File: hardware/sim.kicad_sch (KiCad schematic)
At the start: 11 parts, among them J12 PRPC006SAAN-RC, J13 SIM8070-6-0-11-00-A

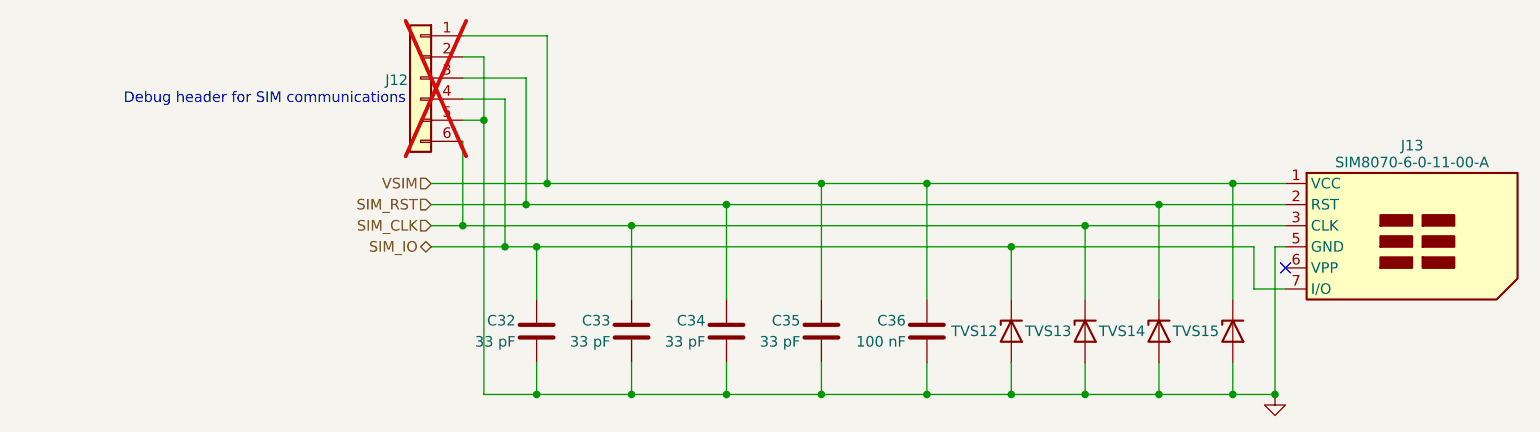
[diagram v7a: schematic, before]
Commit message: HW: Update components, change footprints to handsolder versions, finish power
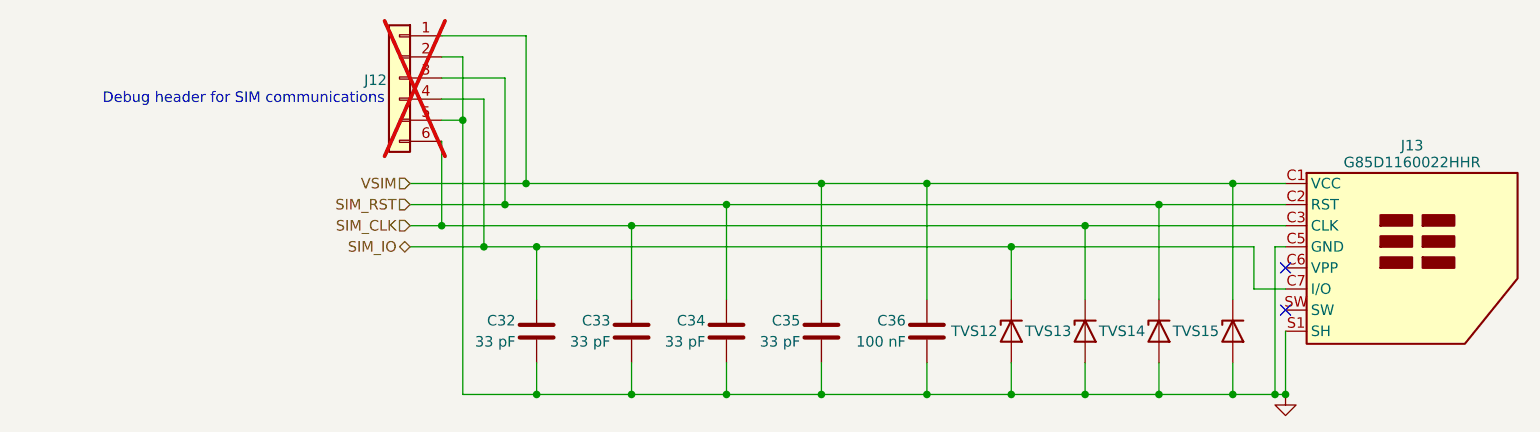
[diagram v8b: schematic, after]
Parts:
- J13: value SIM8070-6-0-11-00-A -> G85D1160022HHR; footprint SIM8070-6-0-11-00-A:SIM8070-6-0-11-00-A -> G85D1160022HHR:AMPHENOL_G85D1160022HHR; Digi-Key Part Number 2073-SIM8070-6-0-11-00-ACT-ND -> 664-G85D1160022HHRCT-ND; Manufacturer GCT -> Amphenol ICC (Commercial Products); Manufacturer Part Number SIM8070-6-0-11-00-A -> G85D1160022HHR
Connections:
- net GND: now also J13.C5 (GND), J13.S1 (SH), J13.S2 (SH), J13.S3 (SH); no longer J13.5 (GND)
- net SIM_CLK: now also J13.C3 (CLK); no longer J13.3 (CLK)
- net SIM_IO: now also J13.C7 (I/O); no longer J13.7 (I/O)
- net SIM_RST: now also J13.C2 (RST); no longer J13.2 (RST)
- net VSIM: now also J13.C1 (VCC); no longer J13.1 (VCC)
- no-connect marks 1 -> 2
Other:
- moved on the sheet: J12
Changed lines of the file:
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@@
 	)
 	(junction
-		(at 92.71 111.76)
+		(at 90.17 111.76)
+		(diameter 0)
+		(color 0 0 0 0)
+	)
+	(junction
+		(at 95.25 121.92)
 		(diameter 0)
 		(color 0 0 0 0)
@@
 	)
 	(junction
-		(at 97.79 121.92)
+		(at 92.71 127)
 		(diameter 0)
 		(color 0 0 0 0)
 	)
 	(junction
-		(at 100.33 119.38)
+		(at 97.79 119.38)
 		(diameter 0)
 		(color 0 0 0 0)
 	)
 	(junction
-		(at 95.25 127)
+		(at 133.35 144.78)
 		(diameter 0)
 		(color 0 0 0 0)
 	)
 	(junction
-		(at 133.35 144.78)
+		(at 182.88 119.38)
 		(diameter 0)
 		(color 0 0 0 0)
 	)
 	(junction
-		(at 182.88 119.38)
+		(at 87.63 124.46)
 		(diameter 0)
 		(color 0 0 0 0)
 	)
 	(junction
-		(at 90.17 124.46)
+		(at 189.23 144.78)
 		(diameter 0)
 		(color 0 0 0 0)
@@
 		(at 189.23 129.54)
 	)
+	(no_connect
+		(at 189.23 134.62)
+	)
 	(wire
 		(pts
-			(xy 97.79 106.68) (xy 97.79 121.92)
+			(xy 95.25 106.68) (xy 95.25 121.92)
 		)
 		(stroke
@@
 	(wire
 		(pts
-			(xy 92.71 144.78) (xy 99.06 144.78)
+			(xy 97.79 119.38) (xy 133.35 119.38)
+		)
+		(stroke
+			(width 0)
+			(type default)
+		)
+	)
+	(wire
+		(pts
+			(xy 90.17 144.78) (xy 99.06 144.78)
 		)
 		(stroke
@@
 	(wire
 		(pts
-			(xy 90.17 106.68) (xy 97.79 106.68)
+			(xy 87.63 106.68) (xy 95.25 106.68)
 		)
 		(stroke
@@
 	(wire
 		(pts
-			(xy 86.36 127) (xy 95.25 127)
+			(xy 83.82 127) (xy 92.71 127)
 		)
 		(stroke
@@
 	(wire
 		(pts
-			(xy 90.17 114.3) (xy 90.17 124.46)
+			(xy 87.63 114.3) (xy 87.63 124.46)
 		)
 		(stroke
@@
 	(wire
 		(pts
-			(xy 86.36 119.38) (xy 100.33 119.38)
+			(xy 83.82 119.38) (xy 97.79 119.38)
 		)
 		(stroke
@@
 	(wire
 		(pts
-			(xy 100.33 101.6) (xy 100.33 119.38)
+			(xy 97.79 101.6) (xy 97.79 119.38)
 		)
 		(stroke
@@
 	(wire
 		(pts
-			(xy 100.33 119.38) (xy 133.35 119.38)
-		)
-		(stroke
-			(width 0)
-			(type default)
-		)
-	)
-	(wire
-		(pts
-			(xy 86.36 124.46) (xy 90.17 124.46)
+			(xy 83.82 124.46) (xy 87.63 124.46)
 		)
 		(stroke
@@
 	(wire
 		(pts
-			(xy 95.25 109.22) (xy 95.25 127)
+			(xy 92.71 109.22) (xy 92.71 127)
 		)
 		(stroke
@@
 	(wire
 		(pts
-			(xy 92.71 111.76) (xy 92.71 144.78)
+			(xy 90.17 111.76) (xy 90.17 144.78)
 		)
 		(stroke
@@
 	(wire
 		(pts
-			(xy 90.17 111.76) (xy 92.71 111.76)
+			(xy 87.63 111.76) (xy 90.17 111.76)
 		)
 		(stroke
@@
 	(wire
 		(pts
-			(xy 90.17 104.14) (xy 92.71 104.14)
+			(xy 87.63 104.14) (xy 90.17 104.14)
 		)
 		(stroke
@@
 	(wire
 		(pts
-			(xy 90.17 109.22) (xy 95.25 109.22)
+			(xy 87.63 109.22) (xy 92.71 109.22)
 		)
 		(stroke
@@
 	(wire
 		(pts
-			(xy 92.71 104.14) (xy 92.71 111.76)
+			(xy 90.17 104.14) (xy 90.17 111.76)
 		)
 		(stroke
@@
 	(wire
 		(pts
-			(xy 97.79 121.92) (xy 121.92 121.92)
+			(xy 165.1 144.78) (xy 173.99 144.78)
 		)
 		(stroke
@@
 	(wire
 		(pts
-			(xy 165.1 144.78) (xy 173.99 144.78)
+			(xy 87.63 101.6) (xy 97.79 101.6)
 		)
 		(stroke
@@
 	(wire
 		(pts
-			(xy 90.17 101.6) (xy 100.33 101.6)
+			(xy 189.23 144.78) (xy 187.96 144.78)
 		)
 		(stroke
@@
 	(wire
 		(pts
+			(xy 95.25 121.92) (xy 121.92 121.92)
+		)
+		(stroke
+			(width 0)
+			(type default)
+		)
+	)
+	(wire
+		(pts
 			(xy 173.99 140.97) (xy 173.99 144.78)
 		)
@@
 	(wire
 		(pts
+			(xy 189.23 137.16) (xy 189.23 144.78)
+		)
+		(stroke
+			(width 0)
+			(type default)
+		)
+	)
+	(wire
+		(pts
 			(xy 156.21 144.78) (xy 165.1 144.78)
 		)
@@
 	(wire
 		(pts
-			(xy 95.25 127) (xy 99.06 127)
+			(xy 92.71 127) (xy 99.06 127)
 		)
 		(stroke
@@
 	(wire
 		(pts
-			(xy 90.17 124.46) (xy 110.49 124.46)
+			(xy 87.63 124.46) (xy 110.49 124.46)
 		)
 		(stroke
@@
 	(wire
 		(pts
-			(xy 86.36 121.92) (xy 97.79 121.92)
+			(xy 83.82 121.92) (xy 95.25 121.92)
 		)
 		(stroke
@@
 	(text "Debug header for SIM communications"
 		(exclude_from_sim no)
-		(at 83.312 109.22 0)
+		(at 80.772 109.22 0)
 		(effects
 			(font
@@
 	(hierarchical_label "VSIM"
 		(shape input)
-		(at 86.36 119.38 180)
+		(at 83.82 119.38 180)
 		(fields_autoplaced yes)
 		(effects
@@
 	(hierarchical_label "SIM_RST"
 		(shape input)
-		(at 86.36 121.92 180)
+		(at 83.82 121.92 180)
 		(fields_autoplaced yes)
 		(effects
@@
 	(hierarchical_label "SIM_CLK"
 		(shape input)
-		(at 86.36 124.46 180)
+		(at 83.82 124.46 180)
 		(fields_autoplaced yes)
 		(effects
@@
 	(hierarchical_label "SIM_IO"
 		(shape bidirectional)
-		(at 86.36 127 180)
+		(at 83.82 127 180)
 		(fields_autoplaced yes)
 		(effects
@@
 	(symbol
 		(lib_id "Connector_Generic:Conn_01x06")
-		(at 85.09 106.68 0)
+		(at 82.55 106.68 0)
 		(mirror y)
 		(unit 1)
@@
 		(dnp yes)
 		(property "Reference" "J12"
-			(at 83.566 106.934 0)
+			(at 81.026 106.934 0)
 			(effects
 				(font
@@
 		)
 		(property "Value" "PRPC006SAAN-RC"
-			(at 83.566 108.712 0)
+			(at 81.026 108.712 0)
 			(effects
 				(font
@@
 		)
 		(property "Footprint" "Connector_PinHeader_2.54mm:PinHeader_1x06_P2.54mm_Vertical"
-			(at 85.09 106.68 0)
+			(at 82.55 106.68 0)
 			(effects
 				(font
@@
 		)
 		(property "Datasheet" "~"
-			(at 85.09 106.68 0)
+			(at 82.55 106.68 0)
 			(effects
 				(font
@@
 		)
 		(property "Description" "Generic connector, single row, 01x06, script generated (kicad-library-utils/schlib/autogen/connector/)"
-			(at 85.09 106.68 0)
+			(at 82.55 106.68 0)
 			(effects
 				(font
@@
 		)
 		(property "Digi-Key Part Number" "S1011EC-06-ND"
-			(at 85.09 106.68 0)
+			(at 82.55 106.68 0)
 			(effects
 				(font
@@
 		)
 		(property "Manufacturer" "Sullins Connector Solutions"
-			(at 85.09 106.68 0)
+			(at 82.55 106.68 0)
 			(effects
 				(font
@@
 		)
 		(property "Manufacturer Part Number" "PRPC006SAAN-RC"
-			(at 85.09 106.68 0)
+			(at 82.55 106.68 0)
 			(effects
 				(font
@@
 			)
 		)
-		(property "Value" "SIM8070-6-0-11-00-A"
+		(property "Value" "G85D1160022HHR"
 			(at 204.47 116.84 0)
 			(effects
@@
 			)
 		)
-		(property "Footprint" "SIM8070-6-0-11-00-A:SIM8070-6-0-11-00-A"
+		(property "Footprint" "G85D1160022HHR:AMPHENOL_G85D1160022HHR"
 			(at 201.93 118.11 0)
 			(effects
@@
 			)
 		)
-		(property "Digi-Key Part Number" "2073-SIM8070-6-0-11-00-ACT-ND"
+		(property "Digi-Key Part Number" "664-G85D1160022HHRCT-ND"
 			(at 201.93 127 0)
 			(effects
@@
 			)
 		)
-		(property "Manufacturer" "GCT"
+		(property "Manufacturer" "Amphenol ICC (Commercial Products)"
 			(at 201.93 127 0)
 			(effects
@@
 			)
 		)
-		(property "Manufacturer Part Number" "SIM8070-6-0-11-00-A"
+		(property "Manufacturer Part Number" "G85D1160022HHR"
 			(at 201.93 127 0)
 			(effects
@@
 			)
 		)
-		(pin "1"
+		(pin "C1"
 		)
-		(pin "2"
+		(pin "C2"
 		)
-		(pin "7"
+		(pin "C3"
 		)
-		(pin "3"
+		(pin "C7"
 		)
-		(pin "5"
+		(pin "S1"
 		)
-		(pin "6"
+		(pin "C5"
+		)
+		(pin "C6"
+		)
+		(pin "S3"
+		)
+		(pin "SW"
+		)
+		(pin "S2"
 		)
 		(instances
@@
 	(symbol
 		(lib_id "power:GND")
-		(at 187.96 144.78 0)
+		(at 189.23 144.78 0)
 		(unit 1)
 		(exclude_from_sim no)
@@
 		(dnp no)
 		(fields_autoplaced yes)
-		(property "Reference" "#PWR058"
-			(at 187.96 151.13 0)
+		(property "Reference" "#PWR056"
+			(at 189.23 151.13 0)
 			(effects
 				(font
@@
 		)
 		(property "Value" "GND"
-			(at 187.96 149.86 0)
+			(at 189.23 149.86 0)
 			(effects
 				(font
@@
 		)
 		(property "Footprint" ""
-			(at 187.96 144.78 0)
+			(at 189.23 144.78 0)
 			(effects
 				(font
@@
 		)
 		(property "Datasheet" ""
-			(at 187.96 144.78 0)
+			(at 189.23 144.78 0)
 			(effects
 				(font
@@
 		)
 		(property "Description" "Power symbol creates a global label with name \"GND\" , ground"
-			(at 187.96 144.78 0)
+			(at 189.23 144.78 0)
 			(effects
 				(font
@@
 			(project "iida_devkit"
 				(path "/b12a6e25-97fb-4aba-bc96-af8db389bb9a/33580d9f-a609-4568-baaf-9a29cf2dabcd"
-					(reference "#PWR058")
+					(reference "#PWR056")
 					(unit 1)
 				)
